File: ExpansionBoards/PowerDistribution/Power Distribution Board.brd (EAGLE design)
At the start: 160 x 73.2 mm, 32 parts, among them J1 216571-2002, J10 640445-6, J11 640445-6, J12 640445-2, J13 640445-5, J14 640445-3, J15 216571-2003, J16 640445-8, J2 216571-2005, J3 216571-2005, J4 350211-1, J5 206832-1001, J7 216571-2003, J8 350211-1, J9 640445-6, K1 AHQSS105DM2FA0G, U3 LM338T/NOPB

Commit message: exp board: power distro: change coin door interlock to AC
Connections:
- removed net N$2: J1.1, RT1.1
- new net N$4: J1.2, J2.5
- net LINE_HOT: now also J1.1; no longer J2.5
- net N$1: now also RT1.1; no longer J1.2
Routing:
- net N$2: track 33.0 -> 0.00 mm
- net N$1: track 15.1 -> 43.9 mm
- net LINE_HOT: track 121.1 -> 147.0 mm
- net N$4: track 0.00 -> 24.0 mm
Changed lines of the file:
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@@
 <contactref element="J3" pad="5"/>
 <contactref element="K1" pad="3"/>
-<wire x1="125.644" y1="6.648" x2="123.468" y2="4.472" width="1.778" layer="1"/>
-<wire x1="123.468" y1="4.472" x2="109.22" y2="4.572" width="1.778" layer="1"/>
-<wire x1="106.872" y1="8.128" x2="106.872" y2="6.92" width="1.778" layer="1"/>
-<wire x1="106.872" y1="6.92" x2="108.966" y2="4.826" width="1.778" layer="1"/>
-<wire x1="108.966" y1="4.826" x2="109.22" y2="4.572" width="1.778" layer="1"/>
-<wire x1="106.934" y1="2.794" x2="108.966" y2="4.826" width="1.778" layer="1"/>
-<contactref element="J2" pad="5"/>
-<wire x1="125.644" y1="6.648" x2="125.644" y2="8.128" width="1.778" layer="1"/>
 <contactref element="J5" pad="5"/>
 <contactref element="J5" pad="10"/>
@@
 <wire x1="51.7" y1="7.3" x2="43.7" y2="7.3" width="1.778" layer="1"/>
 <wire x1="43.7" y1="7.3" x2="40.6" y2="10.4" width="1.778" layer="1"/>
-<wire x1="106.934" y1="2.794" x2="106.894" y2="2.794" width="1.778" layer="1"/>
-<wire x1="106.894" y1="2.794" x2="106.1" y2="2" width="1.778" layer="1"/>
-<wire x1="106.1" y1="2" x2="55.4" y2="2" width="1.778" layer="1"/>
+<wire x1="144" y1="2" x2="103.3" y2="2" width="1.778" layer="1"/>
+<wire x1="103.3" y1="2" x2="55.4" y2="2" width="1.778" layer="1"/>
 <wire x1="55.4" y1="2" x2="51.7" y2="5.7" width="1.778" layer="1"/>
 <wire x1="51.7" y1="7.3" x2="51.7" y2="5.7" width="1.778" layer="1"/>
 <wire x1="40.6" y1="21.956" x2="34.02" y2="28.536" width="1.778" layer="1"/>
+<contactref element="J1" pad="1"/>
+<wire x1="144" y1="2" x2="147.828" y2="5.828" width="1.778" layer="1"/>
+<wire x1="147.828" y1="8.128" x2="147.828" y2="5.828" width="1.778" layer="1"/>
+<wire x1="106.872" y1="8.128" x2="106.872" y2="5.572" width="1.778" layer="1"/>
+<wire x1="106.872" y1="5.572" x2="103.3" y2="2" width="1.778" layer="1"/>
 </signal>
 <signal name="LINE_NEUTRAL">
@@
 <signal name="N$1">
 <contactref element="J2" pad="2"/>
-<contactref element="J1" pad="2"/>
-<wire x1="134.644" y1="8.128" x2="134.644" y2="6.302" width="1.778" layer="1"/>
-<wire x1="134.644" y1="6.302" x2="136.374" y2="4.572" width="1.778" layer="1"/>
-<wire x1="136.374" y1="4.572" x2="142.748" y2="4.572" width="1.778" layer="1"/>
-<wire x1="144.828" y1="8.128" x2="144.828" y2="6.652" width="1.778" layer="1"/>
-<wire x1="144.828" y1="6.652" x2="142.748" y2="4.572" width="1.778" layer="1"/>
+<contactref element="RT1" pad="1"/>
+<wire x1="157.48" y1="37.084" x2="157.48" y2="26.38" width="3" layer="1"/>
+<wire x1="157.48" y1="26.38" x2="153.1" y2="22" width="3" layer="1"/>
+<wire x1="153.1" y1="22" x2="143.8" y2="22" width="3" layer="1"/>
+<wire x1="143.8" y1="22" x2="134.644" y2="12.844" width="3" layer="1"/>
+<wire x1="134.644" y1="8.128" x2="134.644" y2="12.844" width="3" layer="1"/>
 </signal>
 <signal name="LINE_HOT_IN">
@@
 <wire x1="23.114" y1="5.334" x2="23.114" y2="17.014" width="1.778" layer="1"/>
 </signal>
-<signal name="N$2">
-<contactref element="J1" pad="1"/>
-<contactref element="RT1" pad="1"/>
-<wire x1="157.48" y1="37.084" x2="157.48" y2="17.78" width="3" layer="1"/>
-<wire x1="157.48" y1="17.78" x2="147.828" y2="8.128" width="3" layer="1"/>
-</signal>
 <signal name="N$3">
 <contactref element="LED1" pad="A"/>
@@
 <wire x1="154.94" y1="60.706" x2="157.734" y2="57.912" width="1.778" layer="1"/>
 </signal>
+<signal name="N$4">
+<contactref element="J2" pad="5"/>
+<contactref element="J1" pad="2"/>
+<wire x1="125.644" y1="8.128" x2="125.644" y2="6.356" width="1.778" layer="1"/>
+<wire x1="125.644" y1="6.356" x2="127.5" y2="4.5" width="1.778" layer="1"/>
+<wire x1="127.5" y1="4.5" x2="142.6" y2="4.5" width="1.778" layer="1"/>
+<wire x1="144.828" y1="8.128" x2="144.828" y2="6.728" width="1.778" layer="1"/>
+<wire x1="142.6" y1="4.5" x2="144.828" y2="6.728" width="1.778" layer="1"/>
+</signal>
 </signals>

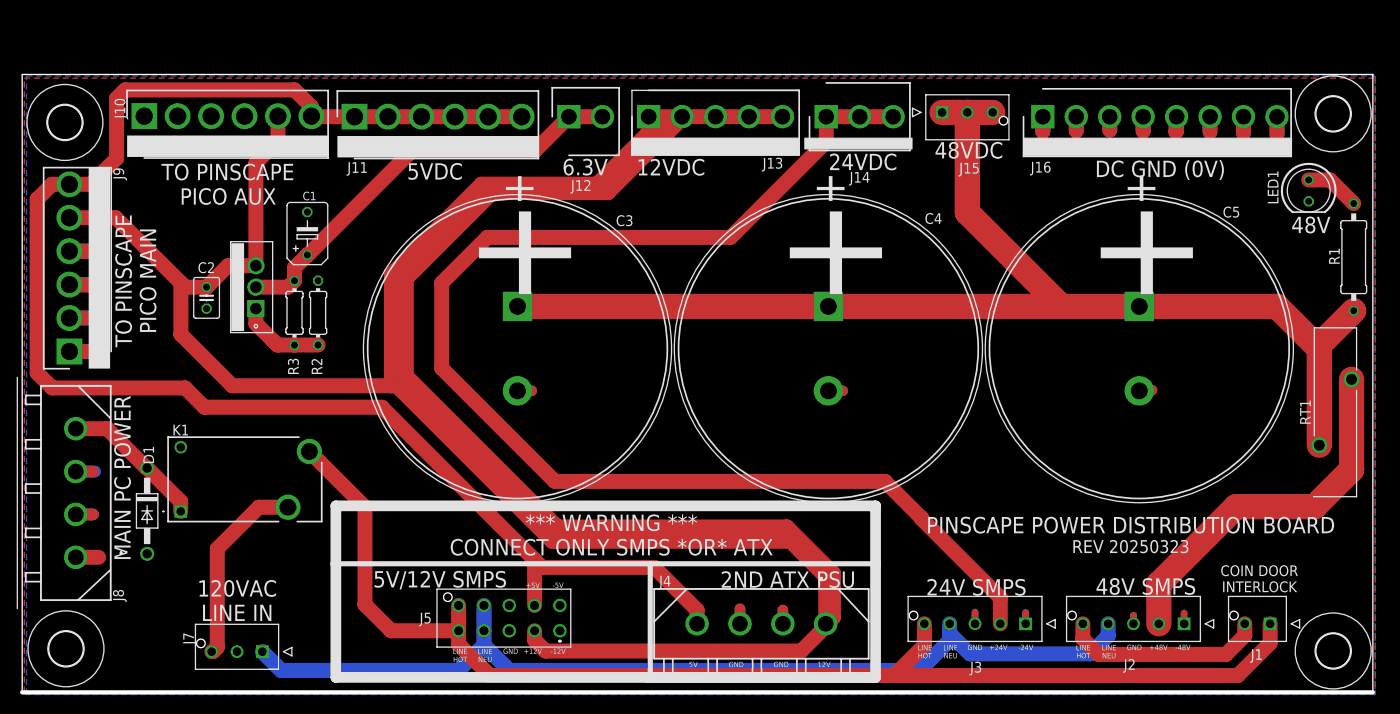
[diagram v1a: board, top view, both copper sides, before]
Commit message: exp board: power distribution: 24-pin ATX connector, 48V interlock via MOSFET, Always On jumper options
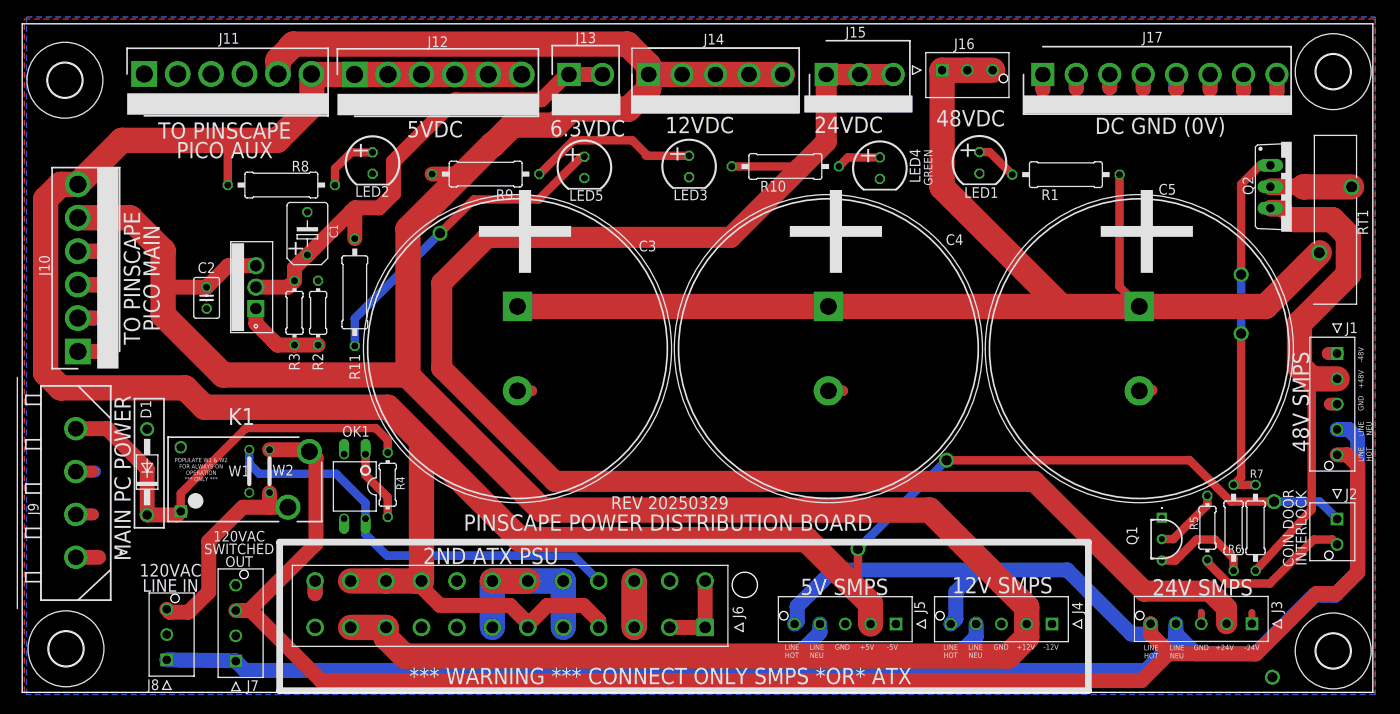
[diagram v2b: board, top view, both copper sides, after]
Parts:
- added J17: 640445-8, SamacSys_Parts:SHDR8W117P0X396_1X8_3170X762X1
- added J6: 44206-0007, SamacSys_Parts:44206-0007_1
- added LED2: Red, led:LED5MM
- added LED3: Yellow, led:LED5MM
- added LED4: Green, led:LED5MM
- added LED5: Orange, led:LED5MM
- added OK1: PC817, optocoupler:DIL04
- added Q1: 2N2222A, SamacSys_Parts:2N2222A
- added Q2: IRF9530, transistor-power:TO220BV
- added R10: 1.1K 1/2W, rcl:0309/12
- added R11: 220R, rcl:0309/12
- added R4: 270R, rcl:0204/7
- added R5: 470R, rcl:0204/7
- added R6: 8.2K, rcl:0207/10
- added R7: 2.2K, rcl:0207/10
- added R8: 150R, rcl:0309/12
- added R9: 510R 1/4W, rcl:0309/12
- added W1, W2: JUMPER-WIRE, SamacSys_Parts:JUMPER-WIRE
- J1: value 216571-2002 -> 216571-2005; device SamacSys_Parts:216571-YY02_1 -> SamacSys_Parts:216571-YY05_1
- J12: value 640445-2 -> 640445-6; device SamacSys_Parts:SHDR2W117P0X396_1X2_792X762X11 -> SamacSys_Parts:SHDR6W183P0X396_1X6_2377X762X1
- J13: value 640445-5 -> 640445-2; device SamacSys_Parts:HDRV5W117P0X396_1X5_1981X762X1 -> SamacSys_Parts:SHDR2W117P0X396_1X2_792X762X11
- J14: value 640445-3 -> 640445-5; device SamacSys_Parts:HDRV3W140P0X396_1X3_1189X762X1 -> SamacSys_Parts:HDRV5W117P0X396_1X5_1981X762X1
- J15: value 216571-2003 -> 640445-3; device SamacSys_Parts:216571-YY03_1 -> SamacSys_Parts:HDRV3W140P0X396_1X3_1189X762X1
- J16: value 640445-8 -> 216571-2003; device SamacSys_Parts:SHDR8W117P0X396_1X8_3170X762X1 -> SamacSys_Parts:216571-YY03_1
- J2: value 216571-2005 -> 216571-2002; device SamacSys_Parts:216571-YY05_1 -> SamacSys_Parts:216571-YY02_1
- J4: value 350211-1 -> 216571-2005; device SamacSys_Parts:3502111 -> SamacSys_Parts:216571-YY05_1
- J5: value 206832-1001 -> 216571-2005; device SamacSys_Parts:2068321001 -> SamacSys_Parts:216571-YY05_1
- J7: value 216571-2003 -> 216571-2004; device SamacSys_Parts:216571-YY03_1 -> SamacSys_Parts:216571-YY04_1
- J8: value 350211-1 -> 216571-2003; device SamacSys_Parts:3502111 -> SamacSys_Parts:216571-YY03_1
- J9: value 640445-6 -> 350211-1; device SamacSys_Parts:SHDR6W183P0X396_1X6_2377X762X1 -> SamacSys_Parts:3502111
- LED1: value (none) -> Blue
- moved J5 39.8 mm to (103.5, 8.10)
- moved LED1 39.1 mm to (113.4, 62.7)
- moved R1 35.5 mm to (123.6, 61.3), turned to 0 degrees
- moved J1 33.0 mm to (155.8, 40.1), turned to 90 degrees
- moved J10 29.0 mm to (6.59, 40.4), turned to 90 degrees
- moved J4 26.8 mm to (122.0, 8.10)
- moved J3 26.8 mm to (145.7, 8.13)
- moved J12 25.9 mm to (39.4, 73.2)
- moved J11 25.4 mm to (14.5, 73.3)
- moved J9 24.4 mm to (6.35, 16.0), turned to 270 degrees
- moved RT1 22.8 mm to (157.5, 59.9)
- moved J2 22.0 mm to (155.8, 20.5), turned to 90 degrees
- moved J13 18.1 mm to (64.8, 73.2), turned to 0 degrees
- moved J8 16.2 mm to (17.1, 3.85)
- moved J15 14.4 mm to (95.2, 73.2), turned to 0 degrees
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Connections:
- new net -12V: J6.14
- new net 3V3: J6.1, J6.13, J6.2
- new net 3V3_1: J6.12
- new net 5V_STANDBY: J6.9
- new net N$10: LED3.A, R9.1
- new net N$11: LED4.A, R10.1
- new net N$12: LED5.A, R11.1
- new net N$2: Q2.D, RT1.1
- new net N$5: Q2.G, R6.1, R7.2
- new net N$6: Q1.3, R6.2
- new net N$7: Q1.2, R5.1
- new net N$8: J2.2, R5.2
- new net N$9: LED2.A, R8.1
- new net PS_ON#: J6.16, OK1.4, W1.P$2
- new net PWR_OK: J6.8
- net 12V: now also J11.5, J14.1, J14.2, J14.3, J14.4, J14.5, J4.2, J6.10, J6.11, R9.2; no longer J13.1, J13.2, J13.3, J13.4, J13.5, J4.1, J5.2, J9.5
- net 12VPC: now also J9.1; no longer J8.1
- net 24V: now also J15.1, J15.2, J15.3, R10.2; no longer J14.1, J14.2, J14.3
- net 48V: now also J16.1, J16.2, J16.3; no longer J15.1, J15.2, J15.3
- net 5V: now also J12.1, J12.2, J12.3, J12.4, J12.5, J12.6, J2.1, J5.2, J6.21, J6.22, J6.23, J6.4, J6.6, R8.2; no longer J11.1, J11.2, J11.3, J11.4, J11.5, J4.4, J5.7, J9.6
- net 5VPC: now also J9.4, R4.2; no longer J8.4
- net 6V3: now also J13.1, J13.2, R11.2; no longer J12.1, J12.2
- net GND: now also J1.1, J1.3, J11.1, J11.2, J11.3, J11.4, J17.1, J17.2, J17.3, J17.4, J17.5, J17.6, J17.7, J17.8, J4.1, J6.15, J6.17, J6.18, J6.19, J6.24, J6.3, J6.5, J6.7, LED2.K, LED3.K, LED4.K, LED5.K, OK1.2, OK1.3, Q1.1, W1.P$1; no longer J16.1, J16.2, J16.3, J16.4, J16.5, J16.6, J16.7, J16.8, J2.1, J2.3, J4.2, J5.6, J5.8, J8.3, J9.1, J9.4
- net LINE_HOT: now also J1.5, J4.5, J7.3, W2.P$2; no longer J1.1, J5.10
- net LINE_HOT_IN: now also J8.3, W2.P$1; no longer J7.3
- net LINE_NEUTRAL: now also J1.4, J4.4, J8.1; no longer J2.4, J5.9
- net N$1: now also J1.2, Q2.S, R7.1; no longer J2.2, RT1.1
- net N$4: now also OK1.1, R4.1; no longer J1.2, J2.5
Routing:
- net 5V: track 186.3 -> 322.9 mm, vias 0 -> 3
- net LINE_HOT: track 147.0 -> 246.9 mm
- net LINE_NEUTRAL: track 115.0 -> 183.2 mm
- net PS_ON#: track 0.00 -> 51.0 mm
- net N$5: track 0.00 -> 43.0 mm, vias 0 -> 2
- net 24V: track 154.1 -> 193.2 mm
- net N$12: track 0.00 -> 38.4 mm, vias 0 -> 1
- net 5VPC: track 17.2 -> 52.0 mm
- net GND: track 81.7 -> 111.7 mm, vias 0 -> 1
- net N$10: track 0.00 -> 20.4 mm
- net N$8: track 0.00 -> 19.1 mm
- net 12V: track 374.4 -> 357.4 mm
- net N$4: track 24.0 -> 8.51 mm
- net N$1: track 43.9 -> 58.9 mm
- net N$6: track 0.00 -> 11.9 mm
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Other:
- board size 160 x 73.2 mm -> 160 x 79.2 mm
- board text added: "120VAC SWITCHED OUT"
- board text added: "12V SMPS"
- board text added: "5V SMPS"
- board text added: "6.3VDC"
- board text added: "GREEN"
- board text added: "POPULATE W1 & W2 FOR ALWAYS-ON OPERATION *** ONLY ***"
- board text added: "REV 20250329"
- board text removed: "12V"
- board text removed: "48V"
- board text removed: "5V"
- board text removed: "5V/12V SMPS"
- board text removed: "6.3V"
- board text removed: "REV 20250323"

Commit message: exp board: power distro board tweaks
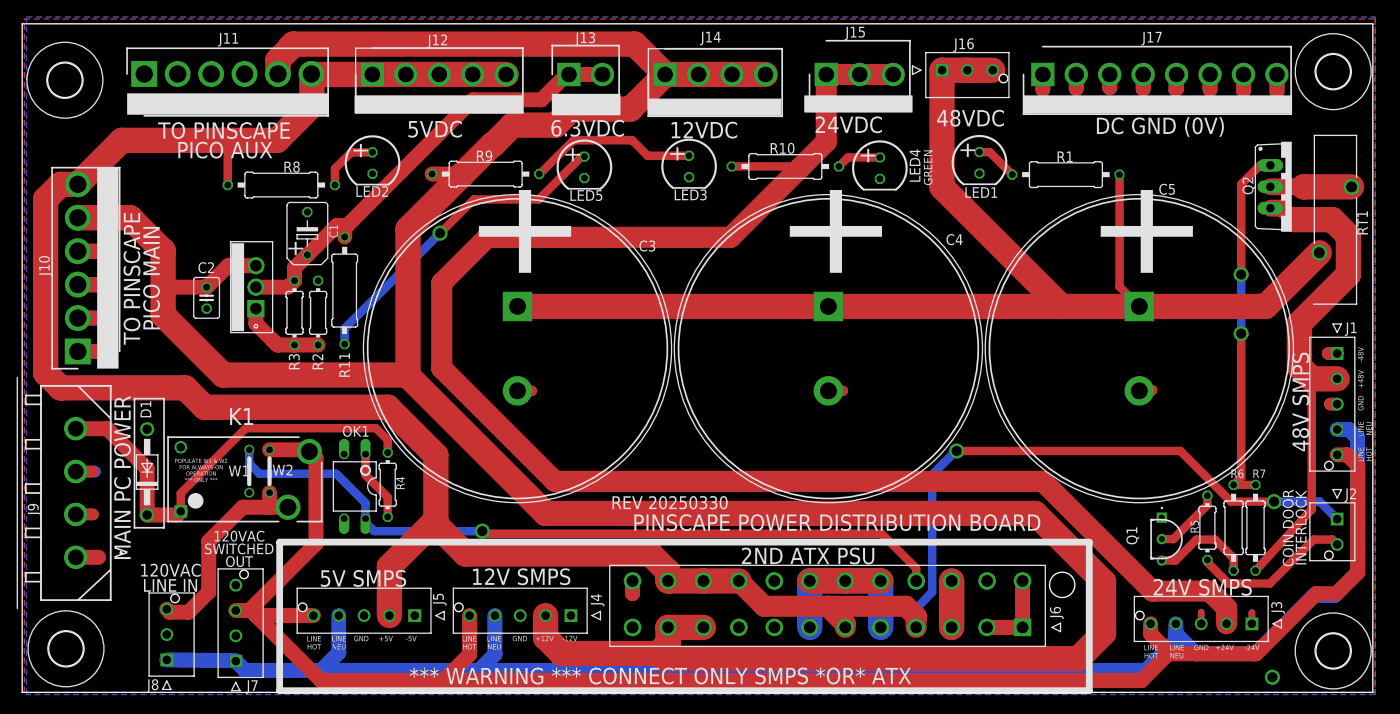
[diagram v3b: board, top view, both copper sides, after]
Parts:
- J12: value 640445-6 -> 640445-5; device SamacSys_Parts:SHDR6W183P0X396_1X6_2377X762X1 -> SamacSys_Parts:HDRV5W117P0X396_1X5_1981X762X1
- J14: value 640445-5 -> 640445-4; device SamacSys_Parts:HDRV5W117P0X396_1X5_1981X762X1 -> SamacSys_Parts:SHDR4W117P0X396_1X4_1585X762X1
- R1: value 2.4K/1W -> 2.4K 1W
- moved J4 57.0 mm to (65.0, 9.10)
- moved J5 57.0 mm to (46.5, 9.10)
- moved J6 37.6 mm to (118.5, 7.70)
- moved J12 10.0 mm to (49.4, 73.2), turned to 180 degrees
- moved R11 1.22 mm to (38.2, 47.6)
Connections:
- net 12V: no longer J14.5
- net 5V: no longer J12.6
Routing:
- net LINE_HOT: track 246.9 -> 204.7 mm
- net PS_ON#: track 51.0 -> 88.6 mm, vias 0 -> 1
- net 5V: track 322.9 -> 298.9 mm, vias 3 -> 2
- net 12V: track 357.4 -> 361.7 mm
- net 6V3: track 58.0 -> 53.8 mm
- net GND: track 111.7 -> 115.8 mm
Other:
- board text added: "REV 20250330"
- board text removed: "REV 20250329"

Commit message: exp board: power distro tweaks
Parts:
- removed J1, J3: 216571-2005, SamacSys_Parts:216571-YY05_1
- added J18, J19: 206832-0601, SamacSys_Parts:2068320601
- moved C4 2.40 mm to (93.1, 45.7)
- moved C5 2.40 mm to (129.9, 45.7)
- moved R11 2.40 mm to (35.8, 47.6)
- moved C2 2.40 mm to (19.4, 46.7)
- moved R3 2.40 mm to (29.9, 45.0)
- moved C3 2.40 mm to (56.3, 45.7)
- moved R2 2.40 mm to (32.7, 45.0)
- moved U3 2.40 mm to (25.3, 45.5)
- moved C1 2.40 mm to (31.4, 54.4)
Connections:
- net 24V: now also J18.5, J18.6; no longer J3.2
- net GND: now also J18.1, J18.4, J19.1, J19.4; no longer J1.1, J1.3, J3.1, J3.3
- net LINE_HOT: now also J18.3, J19.3; no longer J1.5, J3.5
- net LINE_NEUTRAL: now also J18.2, J19.2; no longer J1.4, J3.4
- net N$1: now also J19.5, J19.6; no longer J1.2
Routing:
- net LINE_NEUTRAL: track 183.4 -> 189.9 mm
- net LINE_HOT: track 204.7 -> 210.4 mm
- net GND: track 115.8 -> 121.1 mm
- net 6V3: track 53.8 -> 58.7 mm
- net N$12: track 38.7 -> 42.5 mm
- net 24V: track 193.2 -> 191.0 mm
- net 48V: track 154.0 -> 153.1 mm
- net 12V: track 361.7 -> 362.5 mm
